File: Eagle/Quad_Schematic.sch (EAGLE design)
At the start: 36 parts, among them J1 FTDI_DEVICE, M1 WIRELESS-NRF24L01, U1 ATMEGA328P_TQFP, U2 GY-521MPU6050

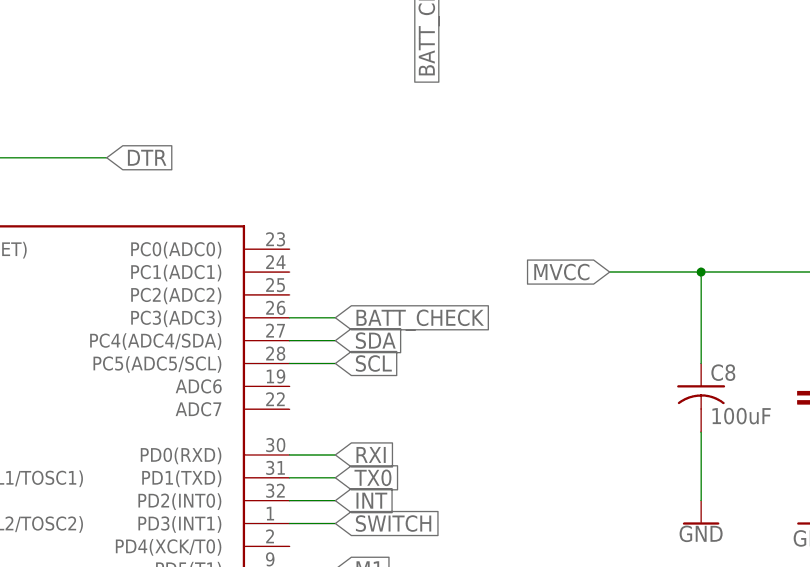
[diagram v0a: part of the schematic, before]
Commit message: 23 airwires left
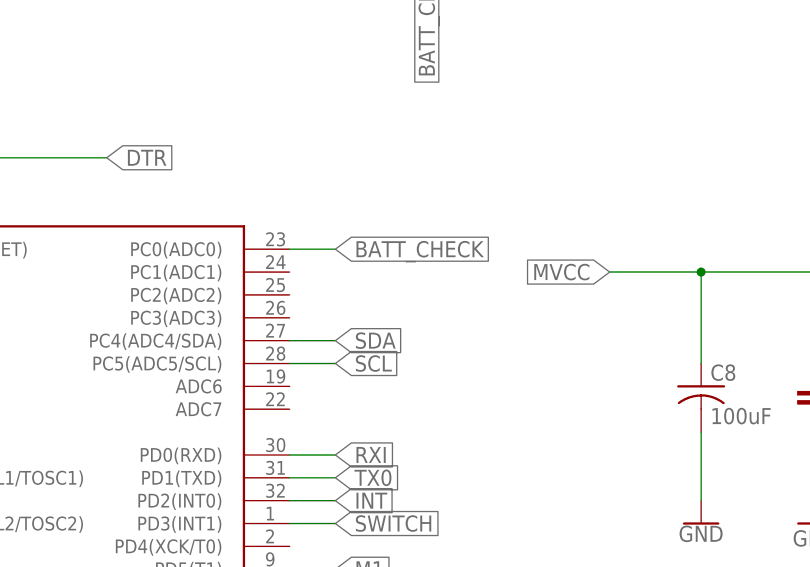
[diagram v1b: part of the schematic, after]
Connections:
- net BATT_CHECK: now also U1.PC0(ADC0); no longer U1.PC3(ADC3)
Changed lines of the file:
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@@
 </segment>
 <segment>
-<pinref part="U1" gate="U$1" pin="PC3(ADC3)"/>
-<wire x1="35.56" y1="129.54" x2="40.64" y2="129.54" width="0.1524" layer="91"/>
-<label x="40.64" y="129.54" size="1.778" layer="95" xref="yes"/>
+<pinref part="U1" gate="U$1" pin="PC0(ADC0)"/>
+<wire x1="35.56" y1="137.16" x2="40.64" y2="137.16" width="0.1524" layer="91"/>
+<label x="40.64" y="137.16" size="1.778" layer="95" xref="yes"/>
 </segment>
 </net>

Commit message: fixed naming and such
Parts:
- renumbered AXR1 to OSC, M1 to RADIO, S1 to SWITCH, S2 to RST, U$1 to NMOS1, U$10 to NMOS4, U$13 to REG, U$4 to NMOS2, U$7 to NMOS3, U1 to ATMEGA
